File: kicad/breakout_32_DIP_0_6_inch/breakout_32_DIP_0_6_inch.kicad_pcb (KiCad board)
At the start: 2 copper layers, 38.1 x 43.7 mm, 3 parts

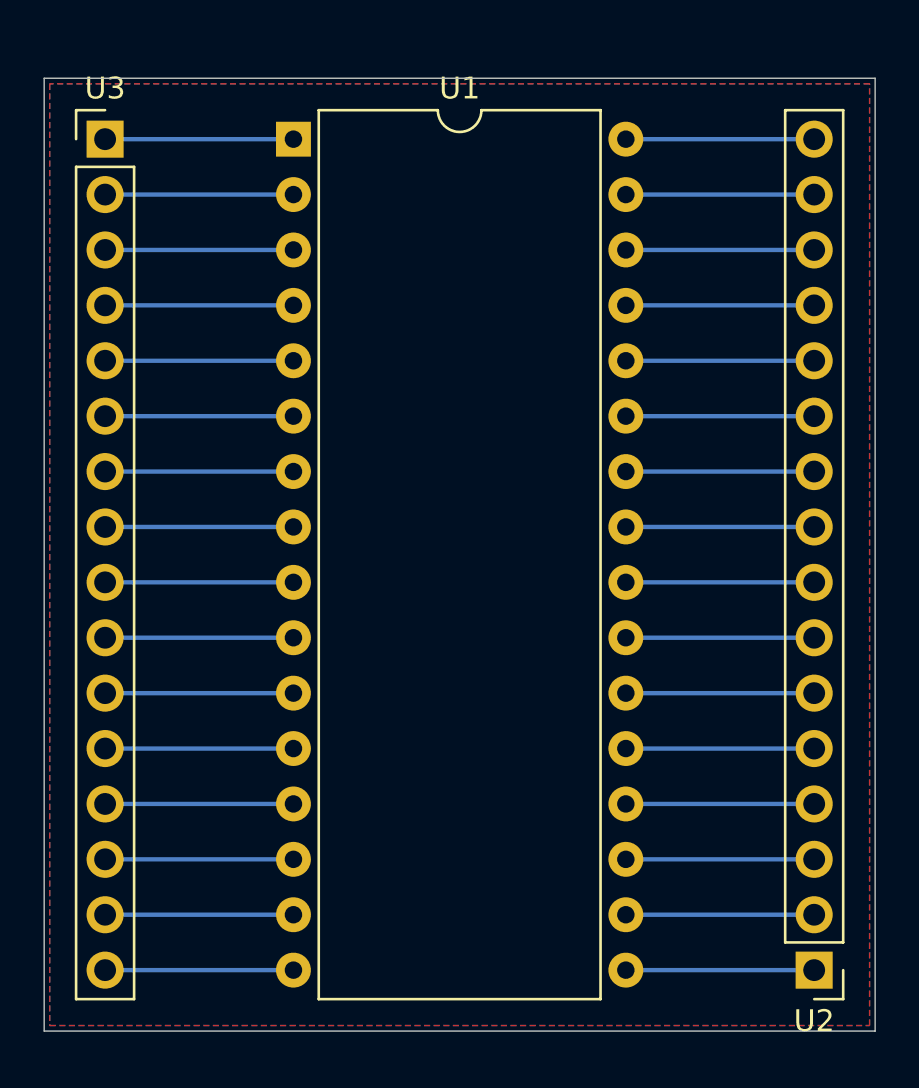
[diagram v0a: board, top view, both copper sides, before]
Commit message: Increased clock PCB clearances
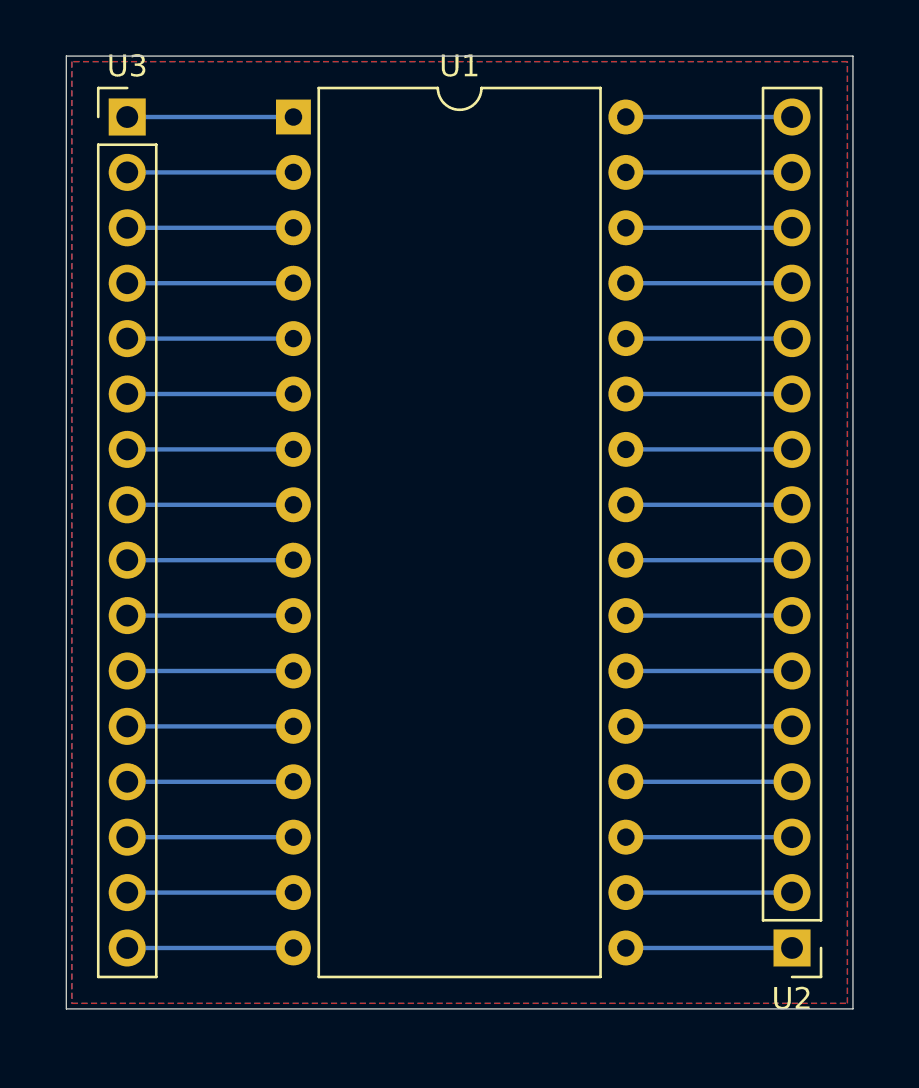
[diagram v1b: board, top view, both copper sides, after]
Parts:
- moved U3 1.44 mm to (132.1, 73.7)
- moved U2 1.44 mm to (162.6, 111.8)
- moved U1 1.02 mm to (139.7, 73.7)
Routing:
- net unconnected-(U1-NC-Pad1): track 8.64 -> 7.62 mm
- net Net-(U1-GND): track 8.64 -> 7.62 mm
- net Net-(U1-DQ2): track 8.64 -> 7.62 mm
- net Net-(U1-DQ1): track 8.64 -> 7.62 mm
- net Net-(U1-DQ0): track 8.64 -> 7.62 mm
- net Net-(U1-A7): track 8.64 -> 7.62 mm
- net Net-(U1-A6): track 8.64 -> 7.62 mm
- net Net-(U1-A5): track 8.64 -> 7.62 mm
- net Net-(U1-A4): track 8.64 -> 7.62 mm
- net Net-(U1-A3): track 8.64 -> 7.62 mm
- net Net-(U1-A2): track 8.64 -> 7.62 mm
- net Net-(U1-A16): track 8.64 -> 7.62 mm
- net Net-(U1-A15): track 8.64 -> 7.62 mm
- net Net-(U1-A12): track 8.64 -> 7.62 mm
- net Net-(U1-A1): track 8.64 -> 7.62 mm
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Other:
- board size 38.1 x 43.7 mm -> 36.1 x 43.7 mm
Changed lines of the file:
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@@
 	(footprint "Connector_PinHeader_2.54mm:PinHeader_1x16_P2.54mm_Vertical"
 		(layer "F.Cu")
-		(at 163.576 112.776 180)
+		(at 162.56 111.76 180)
 		(descr "Through hole straight pin header, 1x16, 2.54mm pitch, single row")
 		(tags "Through hole pin header THT 1x16 2.54mm single row")
@@
 		)
 		(fp_text user "${REFERENCE}"
-			(at 0 19.05 270)
+			(at 0 19.05 -90)
 			(layer "F.Fab")
 			(effects
@@
 	(footprint "Package_DIP:DIP-32_W15.24mm"
 		(layer "F.Cu")
-		(at 139.7 74.676)
+		(at 139.7 73.66)
 		(descr "32-lead though-hole mounted DIP package, row spacing 15.24 mm (600 mils)")
 		(tags "THT DIP DIL PDIP 2.54mm 15.24mm 600mil")
@@
 	(footprint "Connector_PinHeader_2.54mm:PinHeader_1x16_P2.54mm_Vertical"
 		(layer "F.Cu")
-		(at 131.064 74.676)
+		(at 132.08 73.66)
 		(descr "Through hole straight pin header, 1x16, 2.54mm pitch, single row")
 		(tags "Through hole pin header THT 1x16 2.54mm single row")
@@
 	)
 	(gr_rect
-		(start 128.27 71.882)
-		(end 166.37 115.57)
+		(start 129.286 70.866)
+		(end 165.354 114.554)
 		(stroke
 			(width 0.05)
@@
 	)
 	(segment
-		(start 139.7 102.616)
-		(end 131.064 102.616)
+		(start 139.7 101.6)
+		(end 132.08 101.6)
 		(width 0.2)
 		(layer "B.Cu")
@@
 	)
 	(segment
-		(start 154.94 100.076)
-		(end 163.576 100.076)
+		(start 162.56 99.06)
+		(end 154.94 99.06)
 		(width 0.2)
 		(layer "B.Cu")
@@
 	)
 	(segment
-		(start 139.7 92.456)
-		(end 131.064 92.456)
+		(start 139.7 91.44)
+		(end 132.08 91.44)
 		(width 0.2)
 		(layer "B.Cu")
@@
 	)
 	(segment
-		(start 163.576 74.676)
-		(end 154.94 74.676)
+		(start 162.56 73.66)
+		(end 154.94 73.66)
 		(width 0.2)
 		(layer "B.Cu")
@@
 	)
 	(segment
-		(start 154.94 94.996)
-		(end 163.576 94.996)
+		(start 162.56 93.98)
+		(end 154.94 93.98)
 		(width 0.2)
 		(layer "B.Cu")
@@
 	)
 	(segment
-		(start 154.94 77.216)
-		(end 163.576 77.216)
+		(start 154.94 76.2)
+		(end 162.56 76.2)
 		(width 0.2)
 		(layer "B.Cu")
@@
 	)
 	(segment
-		(start 154.94 112.776)
-		(end 163.576 112.776)
+		(start 154.94 111.76)
+		(end 162.56 111.76)
 		(width 0.2)
 		(layer "B.Cu")
@@
 	)
 	(segment
-		(start 131.064 105.156)
-		(end 139.7 105.156)
+		(start 132.08 104.14)
+		(end 139.7 104.14)
 		(width 0.2)
 		(layer "B.Cu")
@@
 	)
 	(segment
-		(start 163.576 92.456)
-		(end 154.94 92.456)
+		(start 154.94 91.44)
+		(end 162.56 91.44)
 		(width 0.2)
 		(layer "B.Cu")
@@
 	)
 	(segment
-		(start 131.064 89.916)
-		(end 139.7 89.916)
+		(start 132.08 88.9)
+		(end 139.7 88.9)
 		(width 0.2)
 		(layer "B.Cu")
@@
 	)
 	(segment
-		(start 163.576 97.536)
-		(end 154.94 97.536)
+		(start 154.94 96.52)
+		(end 162.56 96.52)
 		(width 0.2)
 		(layer "B.Cu")
@@
 	)
 	(segment
-		(start 154.94 84.836)
-		(end 163.576 84.836)
+		(start 162.56 83.82)
+		(end 154.94 83.82)
 		(width 0.2)
 		(layer "B.Cu")
@@
 	)
 	(segment
-		(start 154.94 89.916)
-		(end 163.576 89.916)
+		(start 162.56 88.9)
+		(end 154.94 88.9)
 		(width 0.2)
 		(layer "B.Cu")
@@
 	)
 	(segment
-		(start 131.064 84.836)
-		(end 139.7 84.836)
+		(start 139.7 83.82)
+		(end 132.08 83.82)
 		(width 0.2)
 		(layer "B.Cu")
@@
 	)
 	(segment
-		(start 139.7 112.776)
-		(end 131.064 112.776)
+		(start 139.7 111.76)
+		(end 132.08 111.76)
 		(width 0.2)
 		(layer "B.Cu")
@@
 	)
 	(segment
-		(start 139.7 82.296)
-		(end 131.064 82.296)
+		(start 132.08 81.28)
+		(end 139.7 81.28)
 		(width 0.2)
 		(layer "B.Cu")
@@
 	)
 	(segment
-		(start 131.064 79.756)
-		(end 139.7 79.756)
+		(start 139.7 78.74)
+		(end 132.08 78.74)
 		(width 0.2)
 		(layer "B.Cu")
@@
 	)
 	(segment
-		(start 139.7 97.536)
-		(end 131.064 97.536)
+		(start 139.7 96.52)
+		(end 132.08 96.52)
 		(width 0.2)
 		(layer "B.Cu")
@@
 	)
 	(segment
-		(start 163.576 82.296)
-		(end 154.94 82.296)
+		(start 154.94 81.28)
+		(end 162.56 81.28)
 		(width 0.2)
 		(layer "B.Cu")
@@
 	)
 	(segment
-		(start 163.576 110.236)
-		(end 154.94 110.236)
+		(start 162.56 109.22)
+		(end 154.94 109.22)
 		(width 0.2)
 		(layer "B.Cu")
@@
 	)
 	(segment
-		(start 139.7 74.676)
-		(end 131.064 74.676)
+		(start 139.7 73.66)
+		(end 132.08 73.66)
 		(width 0.2)
 		(layer "B.Cu")
@@
 	)
 	(segment
-		(start 163.576 87.376)
-		(end 154.94 87.376)
+		(start 154.94 86.36)
+		(end 162.56 86.36)
 		(width 0.2)
 		(layer "B.Cu")
@@
 	)
 	(segment
-		(start 163.576 102.616)
-		(end 154.94 102.616)
+		(start 154.94 101.6)
+		(end 162.56 101.6)
 		(width 0.2)
 		(layer "B.Cu")
@@
 	)
 	(segment
-		(start 131.064 110.236)
-		(end 139.7 110.236)
+		(start 132.08 109.22)
+		(end 139.7 109.22)
 		(width 0.2)
 		(layer "B.Cu")
@@
 	)
 	(segment
-		(start 139.7 77.216)
-		(end 131.064 77.216)
+		(start 132.08 76.2)
+		(end 139.7 76.2)
 		(width 0.2)
 		(layer "B.Cu")
@@
 	)
 	(segment
-		(start 139.7 87.376)
-		(end 131.064 87.376)
+		(start 139.7 86.36)
+		(end 132.08 86.36)
 		(width 0.2)
 		(layer "B.Cu")
@@
 	)
 	(segment
-		(start 139.7 107.696)
-		(end 131.064 107.696)
+		(start 139.7 106.68)
+		(end 132.08 106.68)
 		(width 0.2)
 		(layer "B.Cu")
@@
 	)
 	(segment
-		(start 163.576 107.696)
-		(end 154.94 107.696)
+		(start 154.94 106.68)
+		(end 162.56 106.68)
 		(width 0.2)
 		(layer "B.Cu")
@@
 	)
 	(segment
-		(start 131.064 100.076)
-		(end 139.7 100.076)
+		(start 132.08 99.06)
+		(end 139.7 99.06)
 		(width 0.2)
 		(layer "B.Cu")
@@
 	)
 	(segment
-		(start 154.94 105.156)
-		(end 163.576 105.156)
+		(start 162.56 104.14)
+		(end 154.94 104.14)
 		(width 0.2)
 		(layer "B.Cu")
@@
 	)
 	(segment
-		(start 131.064 94.996)
-		(end 139.7 94.996)
+		(start 132.08 93.98)
+		(end 139.7 93.98)
 		(width 0.2)
 		(layer "B.Cu")
@@
 	)
 	(segment
-		(start 154.94 79.756)
-		(end 163.576 79.756)
+		(start 154.94 78.74)
+		(end 162.56 78.74)
 		(width 0.2)
 		(layer "B.Cu")
@@
 		(polygon
 			(pts
-				(xy 128.524 72.136) (xy 128.524 115.316) (xy 166.116 115.316) (xy 166.116 72.136)
-			)
-		)
+				(xy 129.54 71.12) (xy 129.54 114.3) (xy 165.1 114.3) (xy 165.1 71.12)
+			)
+		)
